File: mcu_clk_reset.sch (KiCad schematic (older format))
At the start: 52 parts, among them J4 20021121-00010C4LF, J5 Conn_02x17_Odd_Even, Q3 BSS214NW, Q4 BSS214NW, Q5 BSS214NW, Q6 BSS214NW, U4 IS25WP032D, U5 FE310-G002, X1 KX2132709Z, Y1 TSX-3225 16.0000MF18X-AC0

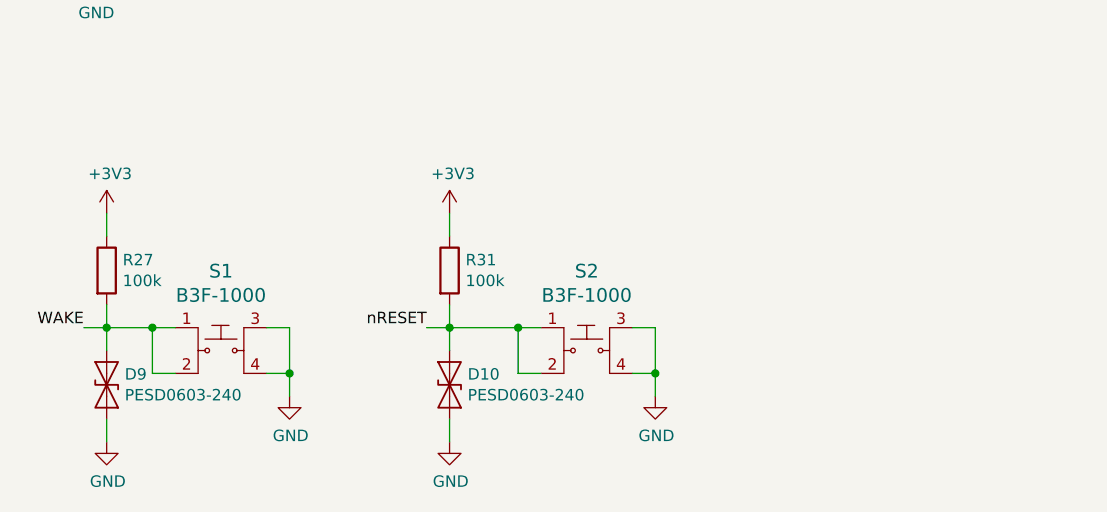
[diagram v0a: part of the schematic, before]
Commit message: Change tactile switches to PTS645
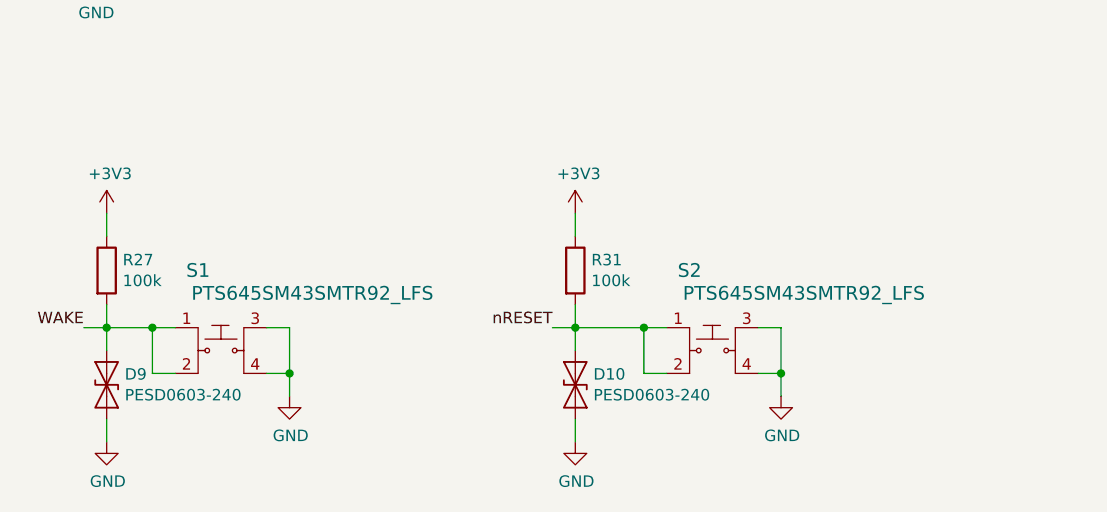
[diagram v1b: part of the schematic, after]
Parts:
- removed S1, S2: B3F-1000, digikey-footprints:Switch_Tactile_THT_B3F-1xxx, symbol dk_Tactile-Switches:B3F-1000
- added S1, S2: PTS645SM43SMTR92_LFS, digikey-footprints:Switch_Tactile_SMD_6x6mm_PTS645, symbol dk_Tactile-Switches:PTS645SM43SMTR92_LFS
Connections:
- net GND: now also S1.3, S1.4, S2.3, S2.4
- net WAKE: now also S1.1, S1.2
- net nRESET: now also S2.1, S2.2
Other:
- moved on the sheet: D10, R31
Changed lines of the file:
@@
 	1450 1200 2400 1200
-$Comp
-L dk_Tactile-Switches:B3F-1000 S1
-U 1 1 5E4118E2
-P 1500 6600
-F 0 "S1" H 1500 6947 60  0000 C CNN
-F 1 "B3F-1000" H 1500 6841 60  0000 C CNN
-F 2 "digikey-footprints:Switch_Tactile_THT_B3F-1xxx" H 1700 6800 60  0001 L CNN
-F 3 "https://omronfs.omron.com/en_US/ecb/products/pdf/en-b3f.pdf" H 1700 6900 60  0001 L CNN
-F 4 "SW400-ND" H 1700 7000 60  0001 L CNN "Digi-Key_PN"
-F 5 "B3F-1000" H 1700 7100 60  0001 L CNN "MPN"
-F 6 "Switches" H 1700 7200 60  0001 L CNN "Category"
-F 7 "Tactile Switches" H 1700 7300 60  0001 L CNN "Family"
-F 8 "https://omronfs.omron.com/en_US/ecb/products/pdf/en-b3f.pdf" H 1700 7400 60  0001 L CNN "DK_Datasheet_Link"
-F 9 "/product-detail/en/omron-electronics-inc-emc-div/B3F-1000/SW400-ND/33150" H 1700 7500 60  0001 L CNN "DK_Detail_Page"
-F 10 "SWITCH TACTILE SPST-NO 0.05A 24V" H 1700 7600 60  0001 L CNN "Description"
-F 11 "Omron Electronics Inc-EMC Div" H 1700 7700 60  0001 L CNN "Manufacturer"
-F 12 "Active" H 1700 7800 60  0001 L CNN "Status"
-	1    1500 6600
-	1    0    0    -1
-$EndComp
 $Comp
 L Device:R R29
@@
 Text Label 900  6500 2    50   ~ 0
 WAKE
-Text Label 2400 6500 2    50   ~ 0
+Text Label 2950 6500 2    50   ~ 0
 nRESET
 Wire Wire Line
@@
 	10200 4500 10400 4500
 $Comp
-L dk_Tactile-Switches:B3F-1000 S2
-U 1 1 5E66799D
-P 3100 6600
-F 0 "S2" H 3100 6947 60  0000 C CNN
-F 1 "B3F-1000" H 3100 6841 60  0000 C CNN
-F 2 "digikey-footprints:Switch_Tactile_THT_B3F-1xxx" H 3300 6800 60  0001 L CNN
-F 3 "https://omronfs.omron.com/en_US/ecb/products/pdf/en-b3f.pdf" H 3300 6900 60  0001 L CNN
-F 4 "SW400-ND" H 3300 7000 60  0001 L CNN "Digi-Key_PN"
-F 5 "B3F-1000" H 3300 7100 60  0001 L CNN "MPN"
-F 6 "Switches" H 3300 7200 60  0001 L CNN "Category"
-F 7 "Tactile Switches" H 3300 7300 60  0001 L CNN "Family"
-F 8 "https://omronfs.omron.com/en_US/ecb/products/pdf/en-b3f.pdf" H 3300 7400 60  0001 L CNN "DK_Datasheet_Link"
-F 9 "/product-detail/en/omron-electronics-inc-emc-div/B3F-1000/SW400-ND/33150" H 3300 7500 60  0001 L CNN "DK_Detail_Page"
-F 10 "SWITCH TACTILE SPST-NO 0.05A 24V" H 3300 7600 60  0001 L CNN "Description"
-F 11 "Omron Electronics Inc-EMC Div" H 3300 7700 60  0001 L CNN "Manufacturer"
-F 12 "Active" H 3300 7800 60  0001 L CNN "Status"
-	1    3100 6600
-	1    0    0    -1
-$EndComp
-$Comp
 L Device:D_TVS D10
 U 1 1 5E6679A3
-P 2500 6750
-F 0 "D10" V 2454 6829 50  0000 L CNN
-F 1 "PESD0603-240" V 2545 6829 50  0000 L CNN
-F 2 "Diode_SMD:D_0603_1608Metric_Pad1.05x0.95mm_HandSolder" H 2500 6750 50  0001 C CNN
-F 3 "~" H 2500 6750 50  0001 C CNN
-	1    2500 6750
+P 3050 6750
+F 0 "D10" V 3004 6829 50  0000 L CNN
+F 1 "PESD0603-240" V 3095 6829 50  0000 L CNN
+F 2 "Diode_SMD:D_0603_1608Metric_Pad1.05x0.95mm_HandSolder" H 3050 6750 50  0001 C CNN
+F 3 "~" H 3050 6750 50  0001 C CNN
+	1    3050 6750
 	0    1    1    0
 $EndComp
 Wire Wire Line
-	3300 6500 3400 6500
-Wire Wire Line
-	3400 6500 3400 6700
-Wire Wire Line
-	3400 6700 3300 6700
+	3850 6500 3950 6500
+Wire Wire Line
+	3950 6500 3950 6700
+Wire Wire Line
+	3950 6700 3850 6700
 $Comp
 L power:GND #PWR038
 U 1 1 5E6679AD
-P 3400 6800
-F 0 "#PWR038" H 3400 6550 50  0001 C CNN
-F 1 "GND" H 3405 6627 50  0000 C CNN
-F 2 "" H 3400 6800 50  0001 C CNN
-F 3 "" H 3400 6800 50  0001 C CNN
-	1    3400 6800
-	1    0    0    -1
-$EndComp
-Wire Wire Line
-	3400 6800 3400 6700
-Connection ~ 3400 6700
-Wire Wire Line
-	2800 6700 2900 6700
+P 3950 6800
+F 0 "#PWR038" H 3950 6550 50  0001 C CNN
+F 1 "GND" H 3955 6627 50  0000 C CNN
+F 2 "" H 3950 6800 50  0001 C CNN
+F 3 "" H 3950 6800 50  0001 C CNN
+	1    3950 6800
+	1    0    0    -1
+$EndComp
+Wire Wire Line
+	3950 6800 3950 6700
+Connection ~ 3950 6700
+Wire Wire Line
+	3350 6700 3450 6700
 $Comp
 L Device:R R31
 U 1 1 5E6679B8
-P 2500 6250
-F 0 "R31" H 2570 6296 50  0000 L CNN
-F 1 "100k" H 2570 6205 50  0000 L CNN
-F 2 "Resistor_SMD:R_0805_2012Metric_Pad1.15x1.40mm_HandSolder" V 2430 6250 50  0001 C CNN
-F 3 "~" H 2500 6250 50  0001 C CNN
-	1    2500 6250
-	1    0    0    -1
-$EndComp
-Wire Wire Line
-	2500 6400 2500 6500
-Connection ~ 2500 6500
-Wire Wire Line
-	2500 6500 2500 6600
-Wire Wire Line
-	2400 6500 2500 6500
+P 3050 6250
+F 0 "R31" H 3120 6296 50  0000 L CNN
+F 1 "100k" H 3120 6205 50  0000 L CNN
+F 2 "Resistor_SMD:R_0805_2012Metric_Pad1.15x1.40mm_HandSolder" V 2980 6250 50  0001 C CNN
+F 3 "~" H 3050 6250 50  0001 C CNN
+	1    3050 6250
+	1    0    0    -1
+$EndComp
+Wire Wire Line
+	3050 6400 3050 6500
+Connection ~ 3050 6500
+Wire Wire Line
+	3050 6500 3050 6600
+Wire Wire Line
+	2950 6500 3050 6500
 $Comp
 L power:GND #PWR034
 U 1 1 5E6679C4
-P 2500 7000
-F 0 "#PWR034" H 2500 6750 50  0001 C CNN
-F 1 "GND" H 2505 6827 50  0000 C CNN
-F 2 "" H 2500 7000 50  0001 C CNN
-F 3 "" H 2500 7000 50  0001 C CNN
-	1    2500 7000
-	1    0    0    -1
-$EndComp
-Wire Wire Line
-	2500 7000 2500 6900
+P 3050 7000
+F 0 "#PWR034" H 3050 6750 50  0001 C CNN
+F 1 "GND" H 3055 6827 50  0000 C CNN
+F 2 "" H 3050 7000 50  0001 C CNN
+F 3 "" H 3050 7000 50  0001 C CNN
+	1    3050 7000
+	1    0    0    -1
+$EndComp
+Wire Wire Line
+	3050 7000 3050 6900
 $Comp
 L power:+3V3 #PWR?
 U 1 1 5E6679CB
-P 2500 6000
+P 3050 6000
 AR Path="/5E6679CB" Ref="#PWR?"  Part="1"
 AR Path="/5E14DB51/5E6679CB" Ref="#PWR033"  Part="1"
-F 0 "#PWR033" H 2500 5850 50  0001 C CNN
-F 1 "+3V3" H 2515 6173 50  0000 C CNN
-F 2 "" H 2500 6000 50  0001 C CNN
-F 3 "" H 2500 6000 50  0001 C CNN
-	1    2500 6000
-	1    0    0    -1
-$EndComp
-Wire Wire Line
-	2500 6000 2500 6100
+F 0 "#PWR033" H 3050 5850 50  0001 C CNN
+F 1 "+3V3" H 3065 6173 50  0000 C CNN
+F 2 "" H 3050 6000 50  0001 C CNN
+F 3 "" H 3050 6000 50  0001 C CNN
+	1    3050 6000
+	1    0    0    -1
+$EndComp
+Wire Wire Line
+	3050 6000 3050 6100
 Wire Wire Line
 	3000 3900 2750 3900
@@
 Connection ~ 5650 2000
 Wire Wire Line
-	2500 6500 2800 6500
-Wire Wire Line
-	2800 6700 2800 6500
-Connection ~ 2800 6500
-Wire Wire Line
-	2800 6500 2900 6500
+	3050 6500 3350 6500
+Wire Wire Line
+	3350 6700 3350 6500
+Connection ~ 3350 6500
+Wire Wire Line
+	3350 6500 3450 6500
+$Comp
+L dk_Tactile-Switches:PTS645SM43SMTR92_LFS S2
+U 1 1 5E1F577A
+P 3650 6600
+F 0 "S2" H 3550 6950 60  0000 C CNN
+F 1 "PTS645SM43SMTR92_LFS" H 4050 6850 60  0000 C CNN
+F 2 "digikey-footprints:Switch_Tactile_SMD_6x6mm_PTS645" H 3850 6800 60  0001 L CNN
+F 3 "https://www.ckswitches.com/media/1471/pts645.pdf" H 3850 6900 60  0001 L CNN
+F 4 "CKN9112CT-ND" H 3850 7000 60  0001 L CNN "Digi-Key_PN"
+F 5 "PTS645SM43SMTR92 LFS" H 3850 7100 60  0001 L CNN "MPN"
+F 6 "Switches" H 3850 7200 60  0001 L CNN "Category"
+F 7 "Tactile Switches" H 3850 7300 60  0001 L CNN "Family"
+F 8 "https://www.ckswitches.com/media/1471/pts645.pdf" H 3850 7400 60  0001 L CNN "DK_Datasheet_Link"
+F 9 "/product-detail/en/c-k/PTS645SM43SMTR92-LFS/CKN9112CT-ND/1146934" H 3850 7500 60  0001 L CNN "DK_Detail_Page"
+F 10 "SWITCH TACTILE SPST-NO 0.05A 12V" H 3850 7600 60  0001 L CNN "Description"
+F 11 "C&K" H 3850 7700 60  0001 L CNN "Manufacturer"
+F 12 "Active" H 3850 7800 60  0001 L CNN "Status"
+	1    3650 6600
+	1    0    0    -1
+$EndComp
+$Comp
+L dk_Tactile-Switches:PTS645SM43SMTR92_LFS S1
+U 1 1 5E1F7DD3
+P 1500 6600
+F 0 "S1" H 1400 6950 60  0000 C CNN
+F 1 "PTS645SM43SMTR92_LFS" H 1900 6850 60  0000 C CNN
+F 2 "digikey-footprints:Switch_Tactile_SMD_6x6mm_PTS645" H 1700 6800 60  0001 L CNN
+F 3 "https://www.ckswitches.com/media/1471/pts645.pdf" H 1700 6900 60  0001 L CNN
+F 4 "CKN9112CT-ND" H 1700 7000 60  0001 L CNN "Digi-Key_PN"
+F 5 "PTS645SM43SMTR92 LFS" H 1700 7100 60  0001 L CNN "MPN"
+F 6 "Switches" H 1700 7200 60  0001 L CNN "Category"
+F 7 "Tactile Switches" H 1700 7300 60  0001 L CNN "Family"
+F 8 "https://www.ckswitches.com/media/1471/pts645.pdf" H 1700 7400 60  0001 L CNN "DK_Datasheet_Link"
+F 9 "/product-detail/en/c-k/PTS645SM43SMTR92-LFS/CKN9112CT-ND/1146934" H 1700 7500 60  0001 L CNN "DK_Detail_Page"
+F 10 "SWITCH TACTILE SPST-NO 0.05A 12V" H 1700 7600 60  0001 L CNN "Description"
+F 11 "C&K" H 1700 7700 60  0001 L CNN "Manufacturer"
+F 12 "Active" H 1700 7800 60  0001 L CNN "Status"
+	1    1500 6600
+	1    0    0    -1
+$EndComp
 $EndSCHEMATC

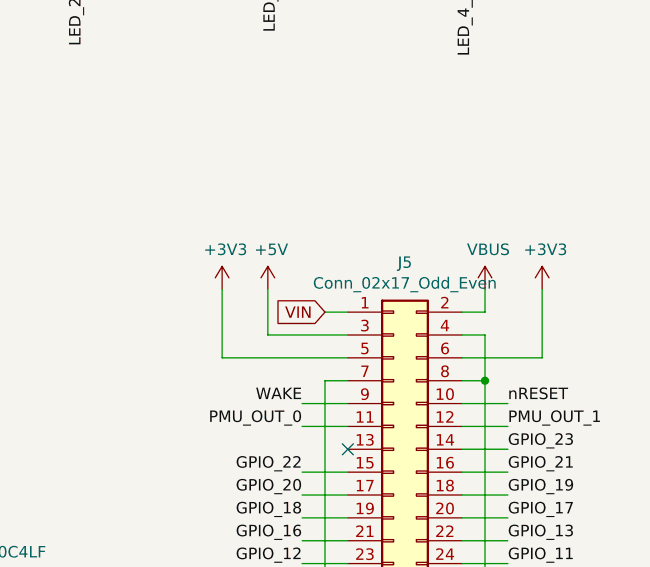
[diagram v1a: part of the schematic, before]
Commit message: Reload netlist, set part number of J1 and J3
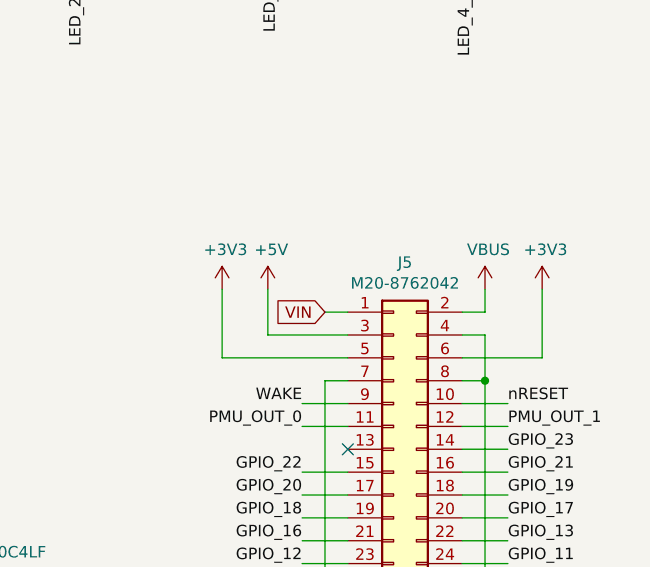
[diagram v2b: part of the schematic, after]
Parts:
- J5: value Conn_02x17_Odd_Even -> M20-8762042
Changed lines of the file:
@@
 P 9900 4900
 F 0 "J5" H 9950 5917 50  0000 C CNN
-F 1 "Conn_02x17_Odd_Even" H 9950 5826 50  0000 C CNN
+F 1 "M20-8762042" H 9950 5826 50  0000 C CNN
 F 2 "Connector_PinHeader_2.54mm:PinHeader_2x17_P2.54mm_Vertical_SMD" H 9900 4900 50  0001 C CNN
 F 3 "~" H 9900 4900 50  0001 C CNN

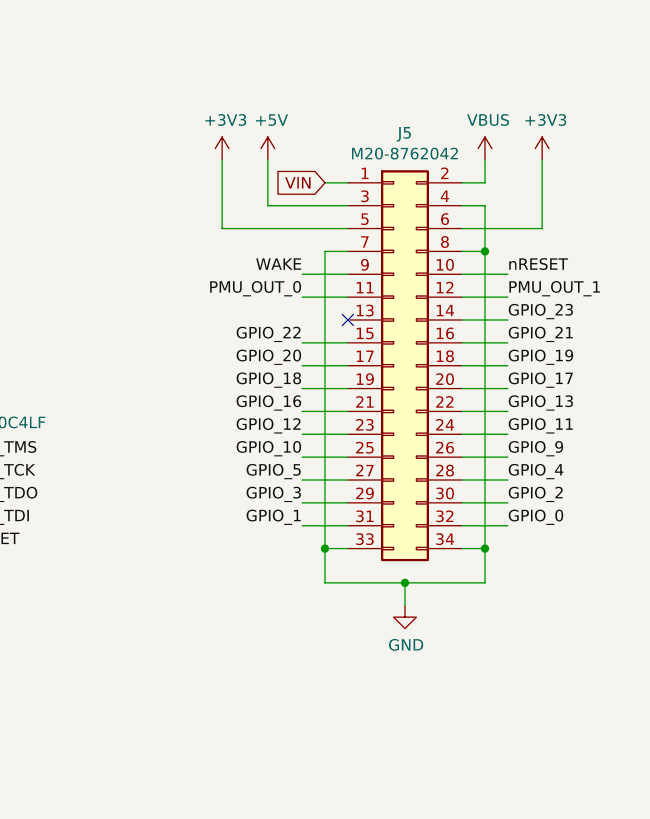
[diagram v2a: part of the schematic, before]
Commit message: Changed main header from 34 to 32 pin, added board outline
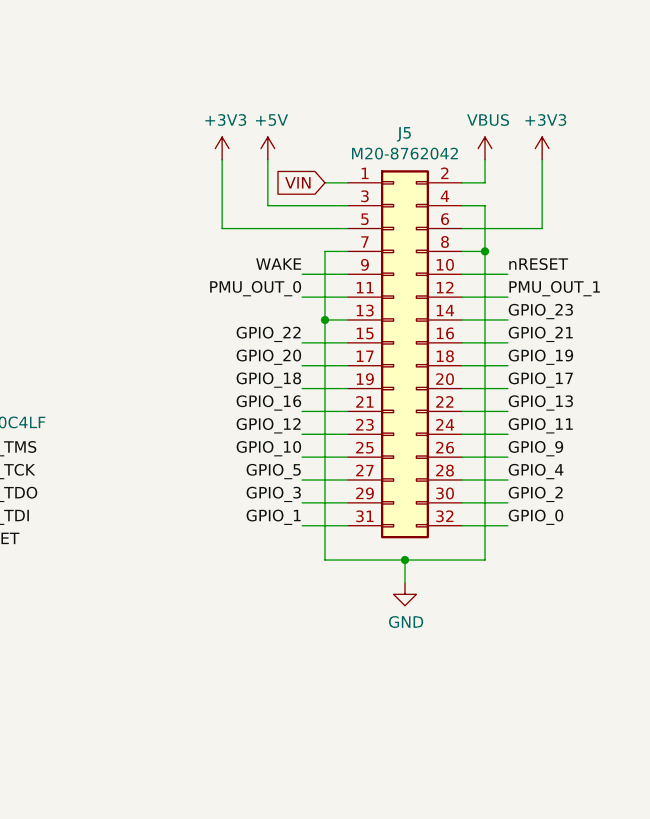
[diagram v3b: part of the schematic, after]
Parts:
- removed J5: M20-8762042, Connector_PinHeader_2.54mm:PinHeader_2x17_P2.54mm_Vertical_SMD, symbol Connector_Generic:Conn_02x17_Odd_Even
- added J5: M20-8762042, Connector_PinHeader_2.54mm:PinHeader_2x16_P2.54mm_Vertical_SMD, symbol Connector_Generic:Conn_02x16_Odd_Even
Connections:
- net +3V3: now also J5.5 (Pin_5), J5.6 (Pin_6)
- net +5V: now also J5.3 (Pin_3)
- net GND: now also J5.13 (Pin_13), J5.4 (Pin_4), J5.7 (Pin_7), J5.8 (Pin_8)
- net GPIO_0: now also J5.32 (Pin_32)
- net GPIO_1: now also J5.31 (Pin_31)
- net GPIO_16: now also J5.21 (Pin_21)
- net GPIO_17: now also J5.20 (Pin_20)
- net GPIO_18: now also J5.19 (Pin_19)
- net GPIO_19: now also J5.18 (Pin_18)
- net GPIO_20: now also J5.17 (Pin_17)
- net GPIO_21: now also J5.16 (Pin_16)
- net GPIO_22: now also J5.15 (Pin_15)
- net GPIO_23: now also J5.14 (Pin_14)
- net I2C_INT: now also J5.24 (Pin_24)
- net I2C_SCL: now also J5.22 (Pin_22)
- net I2C_SDA: now also J5.23 (Pin_23)
- net PMU_OUT_1: now also J5.12 (Pin_12)
- net SPI_CS0: now also J5.30 (Pin_30)
- net SPI_FSYNC: now also J5.25 (Pin_25)
- net SPI_INT: now also J5.26 (Pin_26)
- net SPI_MISO: now also J5.28 (Pin_28)
- net SPI_MOSI: now also J5.29 (Pin_29)
- net SPI_SCK: now also J5.27 (Pin_27)
- net VBUS: now also J5.2 (Pin_2)
- net VDD_CORE_EN: now also J5.11 (Pin_11)
- net VIN: now also J5.1 (Pin_1)
- net WAKE: now also J5.9 (Pin_9)
- net nRESET: now also J5.10 (Pin_10)
- no-connect marks 1 -> 0
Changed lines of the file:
@@
 L power:GND #PWR?
 U 1 1 5E51E4AD
-P 9950 5950
+P 9950 5850
 AR Path="/5E51E4AD" Ref="#PWR?"  Part="1"
 AR Path="/5E14DB51/5E51E4AD" Ref="#PWR054"  Part="1"
-F 0 "#PWR054" H 9950 5700 50  0001 C CNN
-F 1 "GND" H 9955 5777 50  0000 C CNN
-F 2 "" H 9950 5950 50  0001 C CNN
-F 3 "" H 9950 5950 50  0001 C CNN
-	1    9950 5950
-	1    0    0    -1
-$EndComp
-Wire Wire Line
-	9950 5950 9950 5850
-Wire Wire Line
-	9950 5850 10300 5850
-Wire Wire Line
-	9950 5850 9600 5850
-Connection ~ 9950 5850
+F 0 "#PWR054" H 9950 5600 50  0001 C CNN
+F 1 "GND" H 9955 5677 50  0000 C CNN
+F 2 "" H 9950 5850 50  0001 C CNN
+F 3 "" H 9950 5850 50  0001 C CNN
+	1    9950 5850
+	1    0    0    -1
+$EndComp
+Wire Wire Line
+	9950 5850 9950 5750
+Wire Wire Line
+	9950 5750 10300 5750
+Wire Wire Line
+	9950 5750 9600 5750
+Connection ~ 9950 5750
 Wire Wire Line
 	10200 4200 10300 4200
@@
 Wire Wire Line
 	10200 4400 10300 4400
-Connection ~ 10300 4400
 Wire Wire Line
 	9700 4400 9600 4400
@@
 Text Label 10400 4600 0    50   ~ 0
 PMU_OUT_1
-$Comp
-L Connector_Generic:Conn_02x17_Odd_Even J5
-U 1 1 5E8C93BF
-P 9900 4900
-F 0 "J5" H 9950 5917 50  0000 C CNN
-F 1 "M20-8762042" H 9950 5826 50  0000 C CNN
-F 2 "Connector_PinHeader_2.54mm:PinHeader_2x17_P2.54mm_Vertical_SMD" H 9900 4900 50  0001 C CNN
-F 3 "~" H 9900 4900 50  0001 C CNN
-	1    9900 4900
-	1    0    0    -1
-$EndComp
-Wire Wire Line
-	10300 4400 10300 5700
-Wire Wire Line
-	9600 4400 9600 5700
-Wire Wire Line
-	9700 5700 9600 5700
-Connection ~ 9600 5700
-Wire Wire Line
-	9600 5700 9600 5850
-Wire Wire Line
-	10200 5700 10300 5700
-Connection ~ 10300 5700
-Wire Wire Line
-	10300 5700 10300 5850
+Wire Wire Line
+	9600 4400 9600 4700
 Wire Wire Line
 	10400 5600 10200 5600
@@
 Wire Wire Line
 	9700 5600 9500 5600
-NoConn ~ 9700 4700
 Wire Wire Line
 	5600 3800 6100 3800
@@
 	1    0    0    -1
 $EndComp
+$Comp
+L Connector_Generic:Conn_02x16_Odd_Even J5
+U 1 1 5E345E6E
+P 9900 4800
+F 0 "J5" H 9950 5717 50  0000 C CNN
+F 1 "M20-8762042" H 9950 5626 50  0000 C CNN
+F 2 "Connector_PinHeader_2.54mm:PinHeader_2x16_P2.54mm_Vertical_SMD" H 9900 4800 50  0001 C CNN
+F 3 "~" H 9900 4800 50  0001 C CNN
+	1    9900 4800
+	1    0    0    -1
+$EndComp
+Wire Wire Line
+	9600 4700 9700 4700
+Connection ~ 9600 4700
+Wire Wire Line
+	9600 4700 9600 5750
+Wire Wire Line
+	10300 4400 10300 5750
+Connection ~ 10300 4400
 $EndSCHEMATC

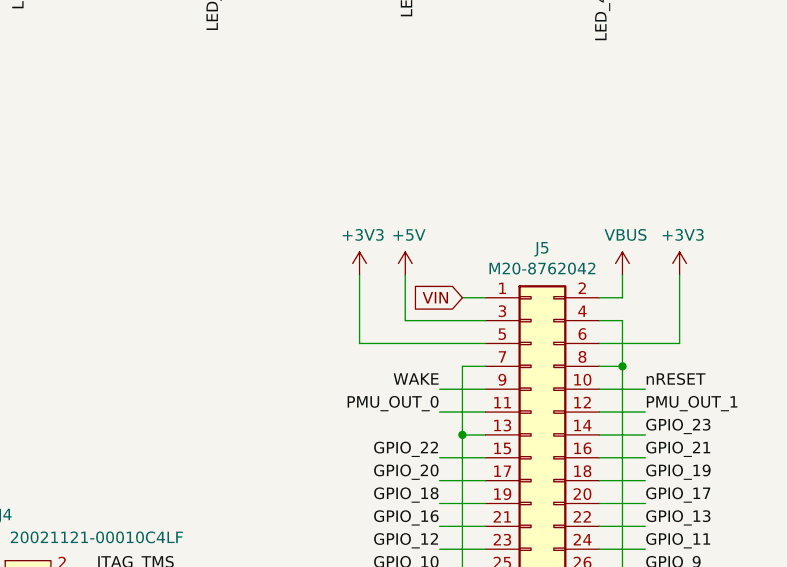
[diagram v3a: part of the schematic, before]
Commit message: Route power traces on the inner layer
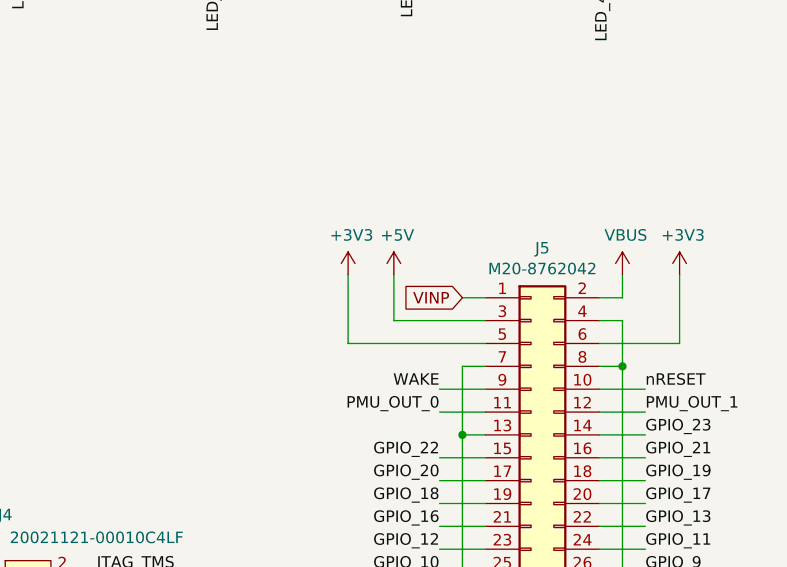
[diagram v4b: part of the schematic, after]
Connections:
- net VIN renamed VINP
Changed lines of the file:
@@
 L power:+5V #PWR051
 U 1 1 5E4DB67D
-P 9350 4000
-F 0 "#PWR051" H 9350 3850 50  0001 C CNN
-F 1 "+5V" H 9365 4173 50  0000 C CNN
-F 2 "" H 9350 4000 50  0001 C CNN
-F 3 "" H 9350 4000 50  0001 C CNN
-	1    9350 4000
+P 9300 4000
+F 0 "#PWR051" H 9300 3850 50  0001 C CNN
+F 1 "+5V" H 9315 4173 50  0000 C CNN
+F 2 "" H 9300 4000 50  0001 C CNN
+F 3 "" H 9300 4000 50  0001 C CNN
+	1    9300 4000
 	1    0    0    -1
 $EndComp
@@
 	10300 4100 10200 4100
 Text GLabel 9600 4100 0    50   Input ~ 0
-VIN
-Wire Wire Line
-	9350 4200 9700 4200
+VINP
 Wire Wire Line
 	10550 4300 10200 4300
@@
 	9700 4400 9600 4400
 Wire Wire Line
-	9350 4000 9350 4200
-Wire Wire Line
 	10550 4000 10550 4300
 $Comp
 L power:+3V3 #PWR050
 U 1 1 5E575B23
-P 9150 4000
-F 0 "#PWR050" H 9150 3850 50  0001 C CNN
-F 1 "+3V3" H 9165 4173 50  0000 C CNN
-F 2 "" H 9150 4000 50  0001 C CNN
-F 3 "" H 9150 4000 50  0001 C CNN
-	1    9150 4000
-	1    0    0    -1
-$EndComp
-Wire Wire Line
-	9150 4000 9150 4300
-Wire Wire Line
-	9150 4300 9700 4300
+P 9100 4000
+F 0 "#PWR050" H 9100 3850 50  0001 C CNN
+F 1 "+3V3" H 9115 4173 50  0000 C CNN
+F 2 "" H 9100 4000 50  0001 C CNN
+F 3 "" H 9100 4000 50  0001 C CNN
+	1    9100 4000
+	1    0    0    -1
+$EndComp
 $Comp
 L Device:D_TVS D9
@@
 	10300 4400 10300 5750
 Connection ~ 10300 4400
+Wire Wire Line
+	9300 4000 9300 4200
+Wire Wire Line
+	9300 4200 9700 4200
+Wire Wire Line
+	9100 4300 9100 4000
+Wire Wire Line
+	9100 4300 9700 4300
 $EndSCHEMATC
